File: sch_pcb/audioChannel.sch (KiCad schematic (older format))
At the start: 80 parts, among them J204 DE9F, Q201 2N7000, Q202 2N7000, Q203 2N7000, U103 MCP4351, U201 MCP6004N, U202 74LVC1G3157, U203 74LVC1G3157, U204 74LVC4066, U205 MCP6004N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

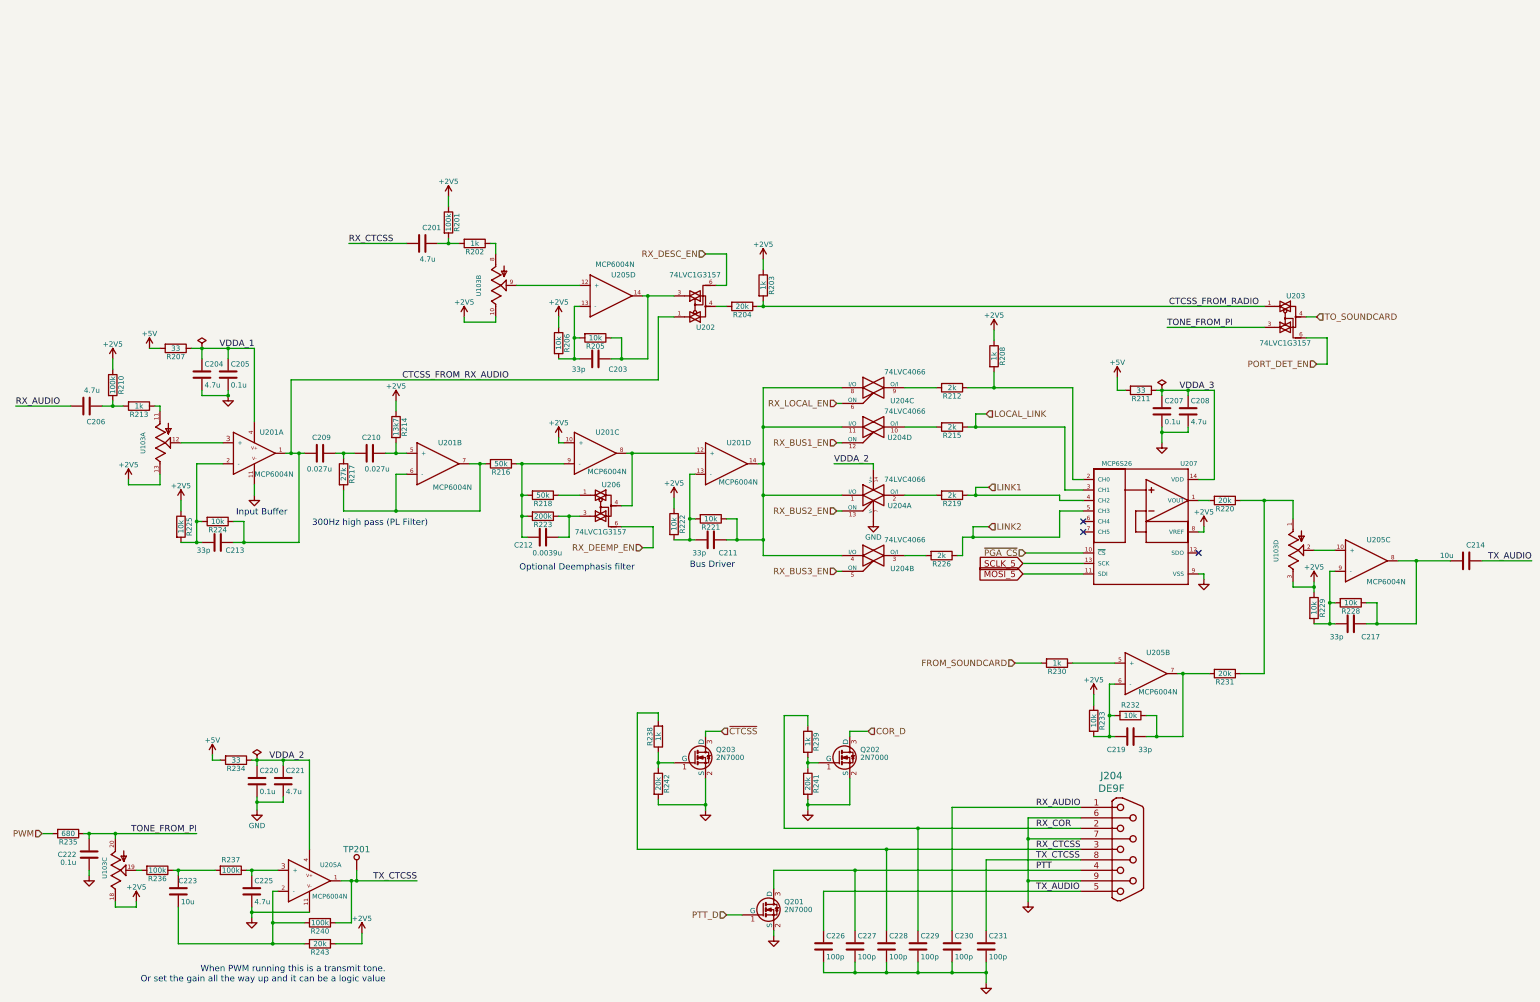
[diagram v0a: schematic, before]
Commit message: Add files via upload
More routing of the PCB....  Slowly getting there.
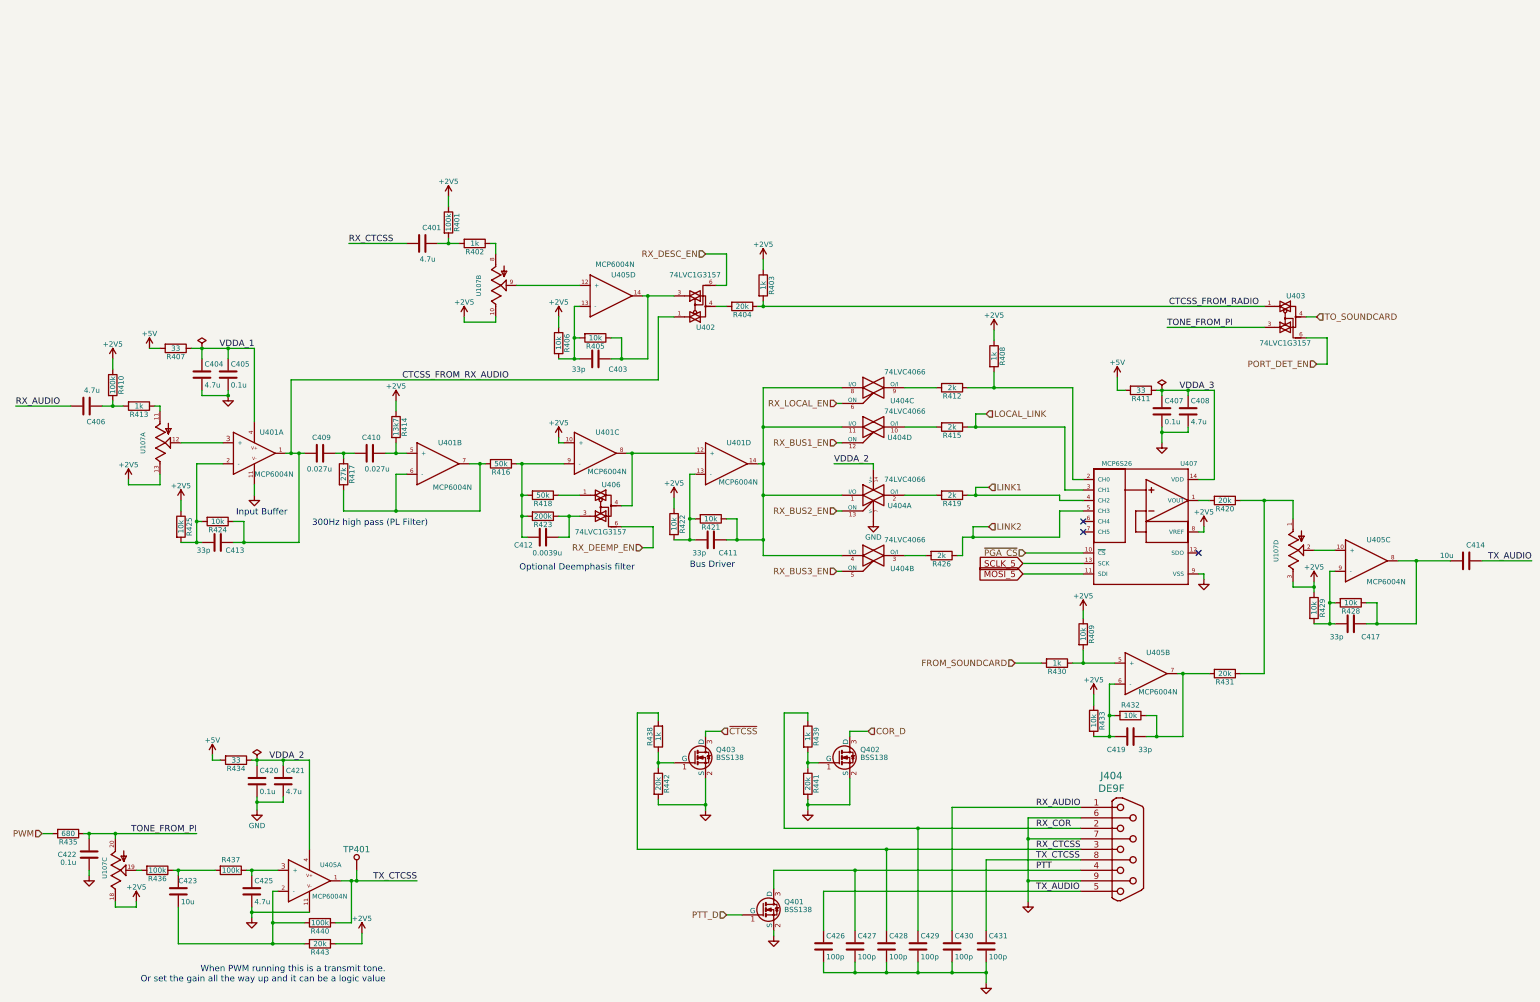
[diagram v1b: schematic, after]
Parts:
- added R209: 10k, lib:smd0603, symbol R
- Q201, Q202, Q203: value 2N7000 -> BSS138
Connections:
- net +2V5: now also R209.1
- net at R230.1, U205.5 (+): now also R209.2
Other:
- moved on the sheet: R439

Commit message: Add files via upload
Add a PMOS switch to allow turning on the soundcard section (hub and 2 soundcard chips) after the Pi has booted.  For some reason, doing so before the desktop loads causes it to hang..
Change gain resistors in opamp stages to move the sweet spot closer to the center of the digital pots to allow for more adjustment range
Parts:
- R205, R224, R228, R232: value 10k -> 100k

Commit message: Update board with third soundcard
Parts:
- added C202, C415: 0.1u, lib:smd0603, symbol C
- added R227, R244: 10k, lib:smd0603, symbol R
- added unit 5 of U103
- added U408: MCP23008, lib:SSOP-20, symbol MCP23008_SSOP20
- U201, U205: value MCP6004N -> MCP6004T
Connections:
- net +5V: now also C202.2, C415.1, R227.2, R244.1, U103.7 (VSS), U408.20 (VCC)
- net GND: now also C202.1, C415.2, U103.17 (VDD), U408.3 (A2), U408.4 (A1), U408.9 (GND)
- net MOSI_5: now also U103.6 (SDI)
- net PORT_DET_EN: now also U408.18 (GP6)
- net RX_BUS1_EN: now also U408.13 (GP1)
- net RX_BUS2_EN: now also U408.14 (GP2)
- net RX_BUS3_EN: now also U408.15 (GP3)
- net RX_DEEMP_EN: now also U408.16 (GP4)
- net RX_DESC_EN: now also U408.17 (GP5)
- net RX_LOCAL_EN: now also U408.12 (GP0)
- net SCLK_5: now also U103.5 (SCK)
- net LINK1 renamed LINK1_AUD
- net LINK2 renamed LINK2_AUD
- net LOCAL_LINK renamed LOCAL_LINK_AUD
- new net: R244.2, U103.15 (~RESET)
- new net: R227.1, U408.6 (~RESET)
- new net I2C_ADDR: U408.5 (A0)
- new net MISO_5: U103.16 (SDO)
- new net SCL1_5: U408.1 (SCL)
- new net SDA1_5: U408.2 (SDA)
- new net ~POT_CS: U103.4 (~CS)
- no-connect marks 3 -> 5

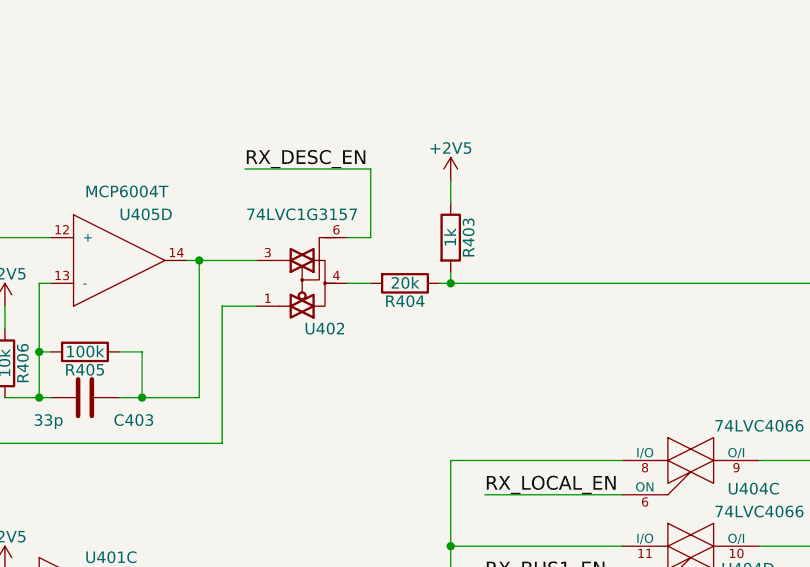
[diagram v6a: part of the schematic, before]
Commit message: Add minimum load on 2v5 regulator.  Update gain to soundcard 1 and 2
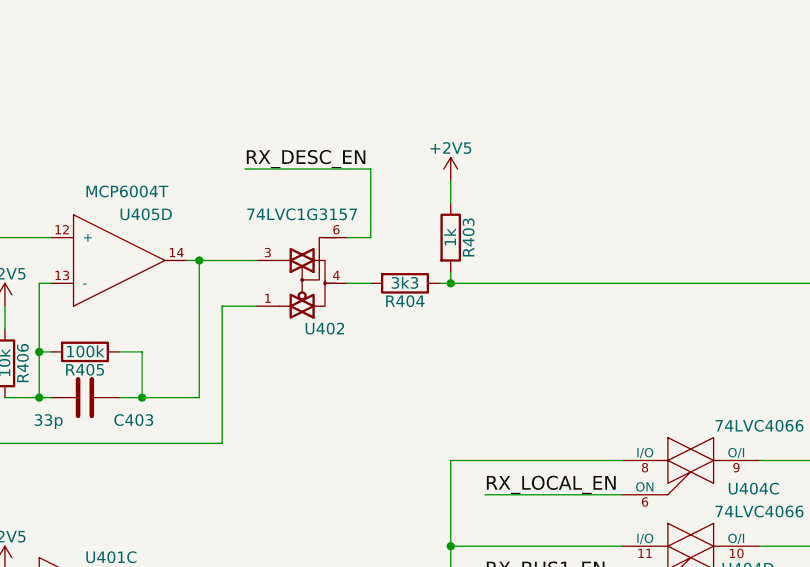
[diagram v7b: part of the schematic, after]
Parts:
- R204: value 20k -> 3k3
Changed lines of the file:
@@
 $Descr B 17000 11000
 encoding utf-8
-Sheet 2 5
+Sheet 4 5
 Title "PiPtr Audio"
 Date ""
@@
 AR Path="/596DD0D0/591CE5B0" Ref="R404"  Part="1"
 F 0 "R404" V 7930 3425 50  0000 C CNN
-F 1 "20k" V 7850 3425 50  0000 C CNN
+F 1 "3k3" V 7850 3425 50  0000 C CNN
 F 2 "lib:smd0603" V 7780 3425 50  0001 C CNN
 F 3 "" H 7850 3425 50  0001 C CNN

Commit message: BOM scrub
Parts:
- R214: value 13k7 -> 13k3
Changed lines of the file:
@@
 AR Path="/596DD0D0/591B655C" Ref="R414"  Part="1"
 F 0 "R414" V 4630 4575 50  0000 C CNN
-F 1 "13k7" V 4550 4575 50  0000 C CNN
+F 1 "13k3" V 4550 4575 50  0000 C CNN
 F 2 "lib:smd0603" V 4480 4575 50  0001 C CNN
 F 3 "" H 4550 4575 50  0001 C CNN
